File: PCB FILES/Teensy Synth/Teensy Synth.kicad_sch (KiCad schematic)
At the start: 102 parts, among them J1 Conn_01x05, SW1 SW_Push, SW10 SW_Push, SW11 SW_Push, SW12 SW_Push, SW13 SW_Push, SW14 SW_Push, SW15 SW_Push, SW16 SW_Push, SW17 SW_Push, SW18 SW_Push, SW19 SW_Push, SW2 SW_Push, SW20 SW_Push, SW21 SW_Push, SW22 SW_Push, SW23 SW_Push, SW24 SW_Push, SW25 SW_Push, SW26 SW_Push, SW27 SW_Push, SW28 SW_Push, SW29 SW_Push, SW3 SW_Push, SW30 SW_Push, SW31 SW_Push, SW32 SW_Push, SW33 SW_Push, SW34 SW_Push, SW35 SW_Push, SW36 SW_Push, SW37 SW_Push, SW38 SW_Push, SW39 SW_Push, SW4 SW_Push, SW40 SW_Push, SW41 SW_Push, SW42 SW_Push, SW43 SW_Push, SW44 SW_Push, SW45 SW_Push, SW46 SW_Push, SW47 SW_Push, SW48 RotaryEncoder, SW49 RotaryEncoder, SW5 SW_Push, SW50 RotaryEncoder, SW51 RotaryEncoder, SW52 RotaryEncoder, SW6 SW_Push, SW7 SW_Push, SW8 SW_Push, SW9 SW_Push, U1 Teensy4.1, U2 RP2040

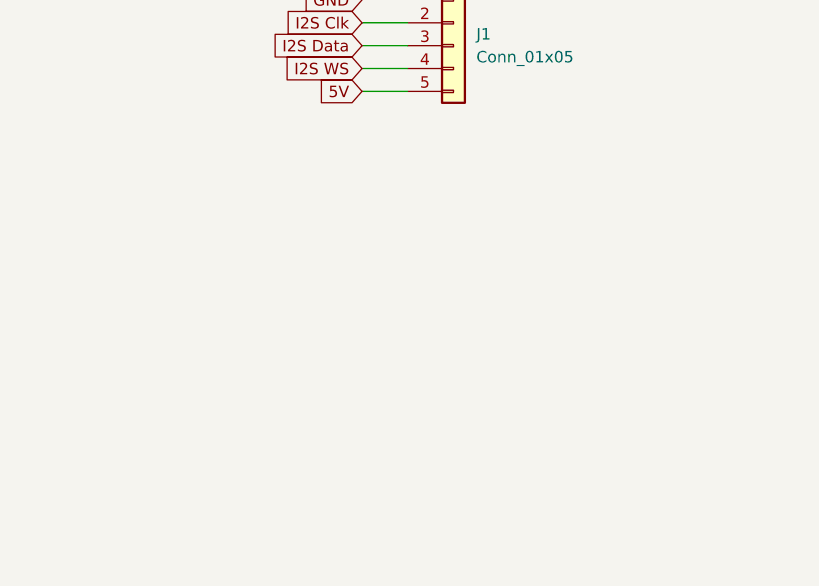
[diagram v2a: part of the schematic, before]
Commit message: Added Screen Pins
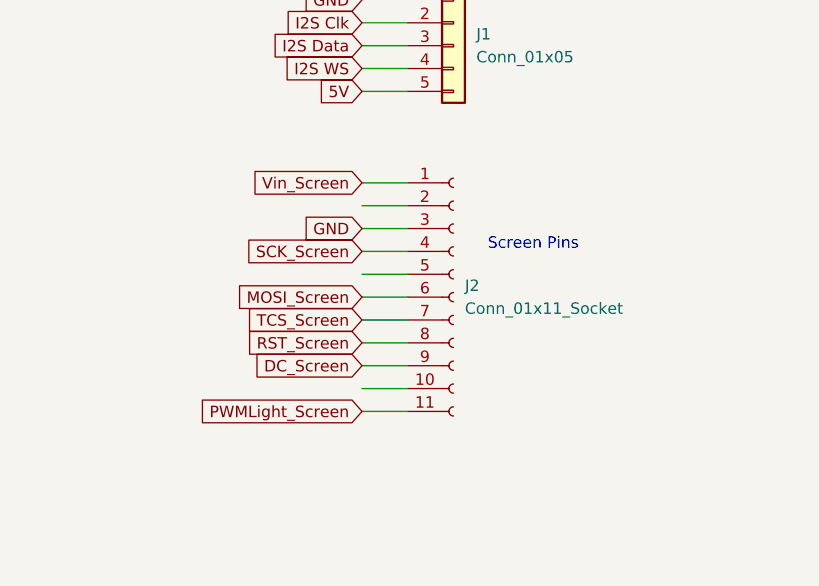
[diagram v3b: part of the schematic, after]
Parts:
- added J2: Conn_01x11_Socket, symbol Connector:Conn_01x11_Socket
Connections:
- net GND: now also J2.3 (Pin_3)
- new net DC_Screen: J2.9 (Pin_9)
- new net MOSI_Screen: J2.6 (Pin_6)
- new net PWMLight_Screen: J2.11 (Pin_11)
- new net RST_Screen: J2.8 (Pin_8)
- new net SCK_Screen: J2.4 (Pin_4)
- new net TCS_Screen: J2.7 (Pin_7)
- new net Vin_Screen: J2.1 (Pin_1)
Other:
- note added: "Screen Pins"
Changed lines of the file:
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@@
   (junction (at 254 330.2) (diameter 0) (color 0 0 0 0)
   )
+  (wire (pts (xy 312.42 63.5) (xy 317.5 63.5))
+    (stroke (width 0) (type default))
+  )
   (wire (pts (xy 86.36 322.58) (xy 86.36 342.9))
     (stroke (width 0) (type default))
@@
     (stroke (width 0) (type default))
   )
+  (wire (pts (xy 312.42 68.58) (xy 317.5 68.58))
+    (stroke (width 0) (type default))
+  )
   (wire (pts (xy 314.96 284.48) (xy 314.96 297.18))
     (stroke (width 0) (type default))
   )
+  (wire (pts (xy 312.42 73.66) (xy 317.5 73.66))
+    (stroke (width 0) (type default))
+  )
   (wire (pts (xy 152.4 304.8) (xy 177.8 304.8))
     (stroke (width 0) (type default))
@@
     (stroke (width 0) (type default))
   )
+  (wire (pts (xy 312.42 76.2) (xy 317.5 76.2))
+    (stroke (width 0) (type default))
+  )
   (wire (pts (xy 177.8 330.2) (xy 203.2 330.2))
     (stroke (width 0) (type default))
@@
     (stroke (width 0) (type default))
   )
+  (wire (pts (xy 312.42 66.04) (xy 317.5 66.04))
+    (stroke (width 0) (type default))
+  )
   (wire (pts (xy 416.56 284.48) (xy 416.56 297.18))
     (stroke (width 0) (type default))
@@
     (stroke (width 0) (type default))
   )
+  (wire (pts (xy 312.42 71.12) (xy 317.5 71.12))
+    (stroke (width 0) (type default))
+  )
   (wire (pts (xy 312.42 40.64) (xy 317.5 40.64))
     (stroke (width 0) (type default))
@@
     (stroke (width 0) (type default))
   )
+  (wire (pts (xy 312.42 78.74) (xy 317.5 78.74))
+    (stroke (width 0) (type default))
+  )
   (wire (pts (xy 365.76 297.18) (xy 365.76 322.58))
     (stroke (width 0) (type default))
@@
     (stroke (width 0) (type default))
   )
+  (wire (pts (xy 312.42 83.82) (xy 317.5 83.82))
+    (stroke (width 0) (type default))
+  )
   (wire (pts (xy 60.96 297.18) (xy 60.96 309.88))
     (stroke (width 0) (type default))
@@
     (stroke (width 0) (type default))
   )
+  (wire (pts (xy 312.42 81.28) (xy 317.5 81.28))
+    (stroke (width 0) (type default))
+  )
   (wire (pts (xy 304.8 330.2) (xy 330.2 330.2))
     (stroke (width 0) (type default))
@@
     (stroke (width 0) (type default))
   )
+  (wire (pts (xy 312.42 60.96) (xy 317.5 60.96))
+    (stroke (width 0) (type default))
+  )
   (wire (pts (xy 50.8 304.8) (xy 76.2 304.8))
     (stroke (width 0) (type default))
@@
     (stroke (width 0) (type default))
   )
+  (wire (pts (xy 312.42 58.42) (xy 317.5 58.42))
+    (stroke (width 0) (type default))
+  )
   (text "To Audio Board" (at 325.12 36.83 0)
     (effects (font (size 1.27 1.27)) (justify left bottom))
   )
+  (text "Screen Pins" (at 326.39 66.04 0)
+    (effects (font (size 1.27 1.27)) (justify left bottom))
+  )
   (global_label "Enc 2A" (shape input) (at 279.4 241.3 270) (fields_autoplaced)
     (effects (font (size 1.27 1.27)) (justify right))
@@
     )
   )
+  (global_label "SCK_Screen" (shape input) (at 312.42 66.04 180) (fields_autoplaced)
+    (effects (font (size 1.27 1.27)) (justify right))
+    (property "Intersheetrefs" "${INTERSHEET_REFS}" (at 298.3072 66.04 0)
+      (effects (font (size 1.27 1.27)) (justify right) hide)
+    )
+  )
   (global_label "Col 13" (shape input) (at 391.16 342.9 270) (fields_autoplaced)
     (effects (font (size 1.27 1.27)) (justify right))
@@
     )
   )
+  (global_label "PWMLight_Screen" (shape input) (at 312.42 83.82 180) (fields_autoplaced)
+    (effects (font (size 1.27 1.27)) (justify right))
+    (property "Intersheetrefs" "${INTERSHEET_REFS}" (at 293.2273 83.82 0)
+      (effects (font (size 1.27 1.27)) (justify right) hide)
+    )
+  )
   (global_label "Col 7" (shape input) (at 238.76 342.9 270) (fields_autoplaced)
     (effects (font (size 1.27 1.27)) (justify right))
@@
     )
   )
+  (global_label "MOSI_Screen" (shape input) (at 312.42 71.12 180) (fields_autoplaced)
+    (effects (font (size 1.27 1.27)) (justify right))
+    (property "Intersheetrefs" "${INTERSHEET_REFS}" (at 297.4605 71.12 0)
+      (effects (font (size 1.27 1.27)) (justify right) hide)
+    )
+  )
+  (global_label "TCS_Screen" (shape input) (at 312.42 73.66 180) (fields_autoplaced)
+    (effects (font (size 1.27 1.27)) (justify right))
+    (property "Intersheetrefs" "${INTERSHEET_REFS}" (at 298.6096 73.66 0)
+      (effects (font (size 1.27 1.27)) (justify right) hide)
+    )
+  )
   (global_label "Enc VA" (shape input) (at 152.4 241.3 270) (fields_autoplaced)
     (effects (font (size 1.27 1.27)) (justify right))
@@
     )
   )
+  (global_label "DC_Screen" (shape input) (at 312.42 78.74 180) (fields_autoplaced)
+    (effects (font (size 1.27 1.27)) (justify right))
+    (property "Intersheetrefs" "${INTERSHEET_REFS}" (at 299.5167 78.74 0)
+      (effects (font (size 1.27 1.27)) (justify right) hide)
+    )
+  )
   (global_label "Enc 3A" (shape input) (at 304.8 241.3 270) (fields_autoplaced)
     (effects (font (size 1.27 1.27)) (justify right))
@@
     )
   )
+  (global_label "Vin_Screen" (shape input) (at 312.42 58.42 180) (fields_autoplaced)
+    (effects (font (size 1.27 1.27)) (justify right))
+    (property "Intersheetrefs" "${INTERSHEET_REFS}" (at 299.2143 58.42 0)
+      (effects (font (size 1.27 1.27)) (justify right) hide)
+    )
+  )
   (global_label "Enc VB" (shape input) (at 157.48 241.3 270) (fields_autoplaced)
     (effects (font (size 1.27 1.27)) (justify right))
@@
     )
   )
+  (global_label "RST_Screen" (shape input) (at 312.42 76.2 180) (fields_autoplaced)
+    (effects (font (size 1.27 1.27)) (justify right))
+    (property "Intersheetrefs" "${INTERSHEET_REFS}" (at 298.6096 76.2 0)
+      (effects (font (size 1.27 1.27)) (justify right) hide)
+    )
+  )
+  (global_label "GND" (shape input) (at 312.42 63.5 180) (fields_autoplaced)
+    (effects (font (size 1.27 1.27)) (justify right))
+    (property "Intersheetrefs" "${INTERSHEET_REFS}" (at 305.5643 63.5 0)
+      (effects (font (size 1.27 1.27)) (justify right) hide)
+    )
+  )
   (global_label "5V" (shape input) (at 312.42 48.26 180) (fields_autoplaced)
     (effects (font (size 1.27 1.27)) (justify right))
@@
         )
       )
+    )
+  )
+  (symbol (lib_id "Connector:Conn_01x11_Socket") (at 322.58 71.12 0) (unit 1)
+    (in_bom yes) (on_board yes) (dnp no) (fields_autoplaced)
+    (property "Reference" "J2" (at 323.85 69.85 0)
+      (effects (font (size 1.27 1.27)) (justify left))
+    )
+    (property "Value" "Conn_01x11_Socket" (at 323.85 72.39 0)
+      (effects (font (size 1.27 1.27)) (justify left))
+    )
+    (property "Footprint" "" (at 322.58 71.12 0)
+      (effects (font (size 1.27 1.27)) hide)
+    )
+    (property "Datasheet" "~" (at 322.58 71.12 0)
+      (effects (font (size 1.27 1.27)) hide)
+    )
+    (pin "1")
+    (pin "10")
+    (pin "11")
+    (pin "2")
+    (pin "3")
+    (pin "4")
+    (pin "5")
+    (pin "6")
+    (pin "7")
+    (pin "8")
+    (pin "9")
+    (instances
+      (project "Teensy Synth"
+        (path "/c9e64777-b068-4bbd-bb2c-e1f5e825559e"
+          (reference "J2") (unit 1)
+        )
+      )

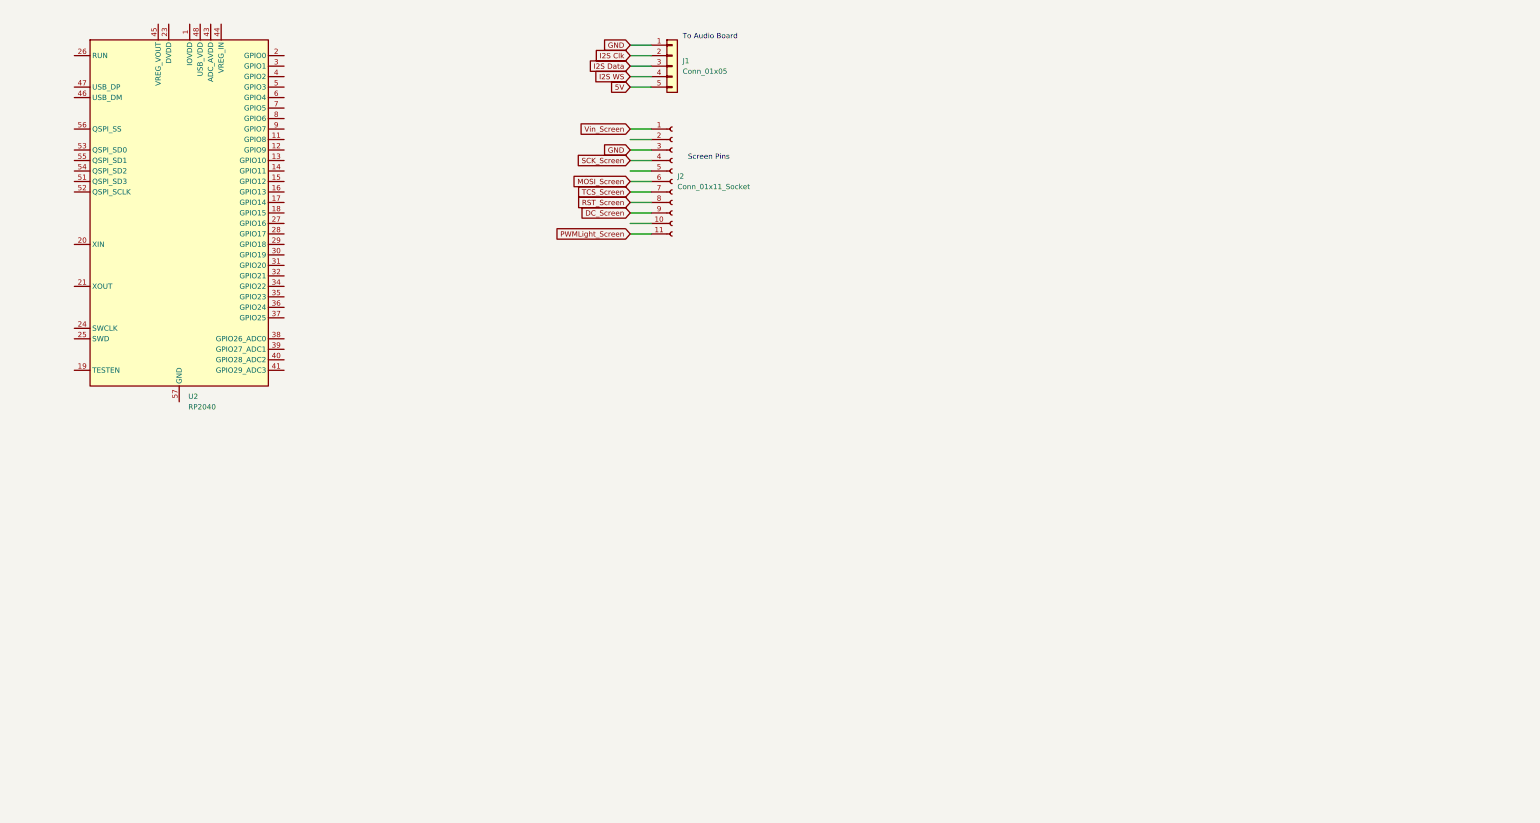
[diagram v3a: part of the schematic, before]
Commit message: Added EncoderDaughterboard and Firmware folders
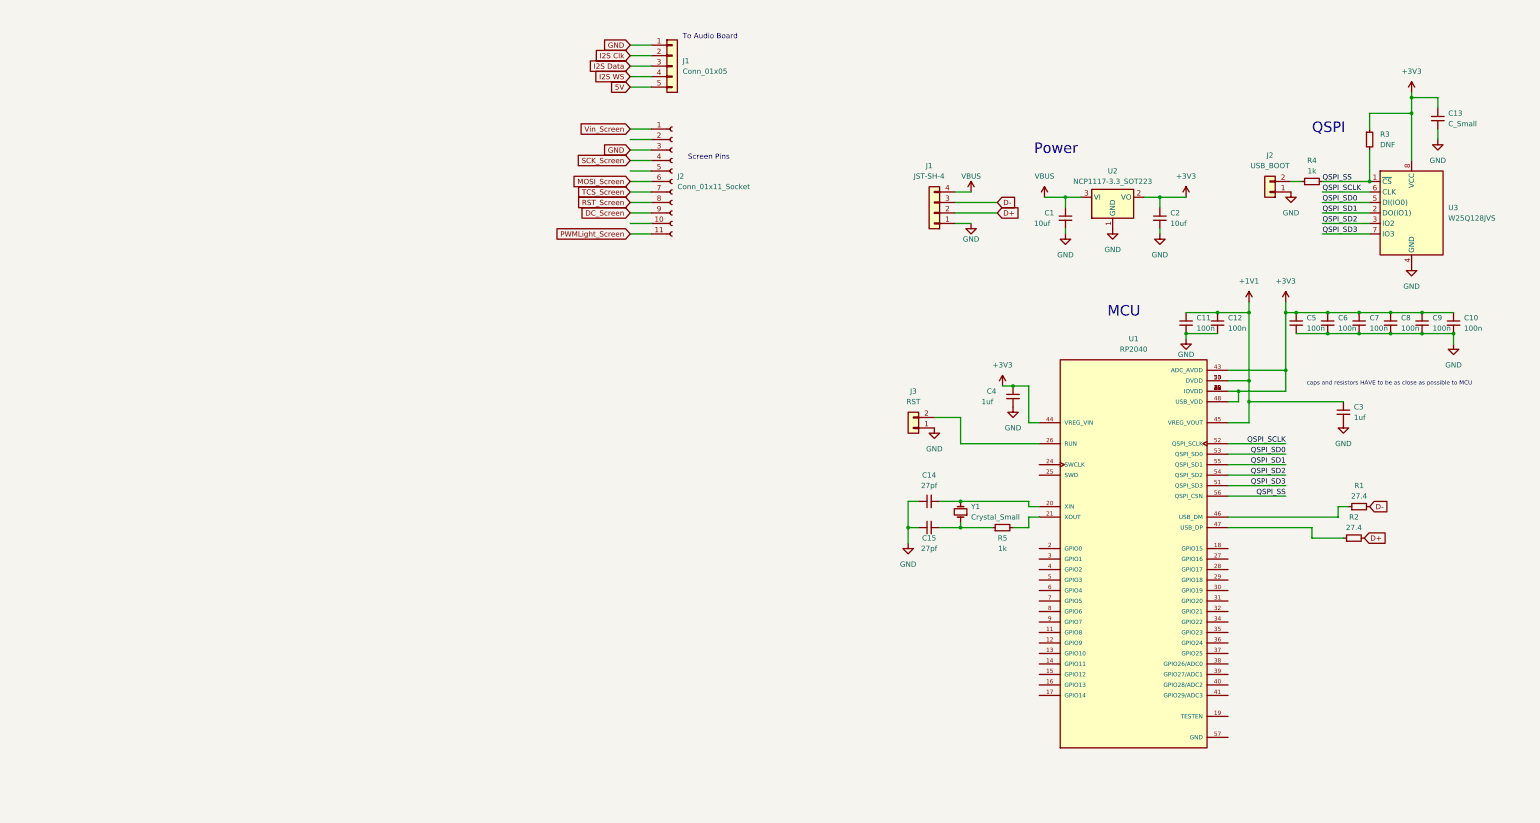
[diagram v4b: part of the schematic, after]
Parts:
- removed U2: RP2040, Package_DFN_QFN:QFN-56-1EP_7x7mm_P0.4mm_EP3.2x3.2mm, symbol MCU_RaspberryPi:RP2040
- added C1, C2: 10uf, symbol Device:C_Small
- added C10, C11, C12, C5, C6, C7, C8, C9: 100n, symbol Device:C_Small
- added C13: C_Small, symbol Device:C_Small
- added C14, C15: 27pf, symbol Device:C_Small
- added C3, C4: 1uf, symbol Device:C_Small
- added J1: JST-SH-4, symbol Connector_Generic:Conn_01x04
- added J2: USB_BOOT, symbol Connector_Generic:Conn_01x02
- added J3: RST, symbol Connector_Generic:Conn_01x02
- added R1, R2: 27.4, symbol Device:R_Small
- added R3: DNF, symbol Device:R_Small
- added R4, R5: 1k, symbol Device:R_Small
- added U1: RP2040, RP2040:QFN40P700X700X90-57N, symbol RP2040:RP2040
- added U2: NCP1117-3.3_SOT223, Package_TO_SOT_SMD:SOT-223-3_TabPin2, symbol Regulator_Linear:NCP1117-3.3_SOT223
- added U3: W25Q128JVS, Package_SO:SOIC-8_5.23x5.23mm_P1.27mm, symbol Memory_Flash:W25Q128JVS
- added Y1: Crystal_Small, symbol Device:Crystal_Small
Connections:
- net GND: now also C1.2, C10.2, C11.2, C12.2, C13.2, C14.1, C15.1, C2.2, C3.2, C4.2, C5.2, C6.2, C7.2, C8.2, C9.2, J1.1 (Pin_1), J2.1 (Pin_1), J3.1 (Pin_1), U2.1 (GND), U3.4 (GND)
- new net: C14.2, U1.20 (XIN), Y1.2
- new net: C15.2, R5.1, Y1.1
- new net: R2.1, U1.47 (USB_DP)
- new net: J3.2 (Pin_2), U1.26 (RUN)
- new net: J2.2 (Pin_2), R4.1
- new net: R5.2, U1.21 (XOUT)
- new net: R1.1, U1.46 (USB_DM)
- new net +1V1: C11.1, C12.1, C3.1, U1.23 (DVDD), U1.45 (VREG_VOUT), U1.50 (DVDD)
- new net +3V3: C10.1, C13.1, C2.1, C4.1, C5.1, C6.1, C7.1, C8.1, C9.1, R3.1, U1.1 (IOVDD), U1.10 (IOVDD), U1.22 (IOVDD), U1.33 (IOVDD), U1.42 (IOVDD), U1.43 (ADC_AVDD), U1.44 (VREG_VIN), U1.48 (USB_VDD), U1.49 (IOVDD), U2.2 (VO), U3.8 (VCC)
- new net D+: J1.2 (Pin_2), R2.2
- new net D-: J1.3 (Pin_3), R1.2
- new net QSPI_SCLK: U1.52 (QSPI_SCLK), U3.6 (CLK)
- new net QSPI_SD0: U1.53 (QSPI_SD0), U3.5 (DI(IO0))
- new net QSPI_SD1: U1.55 (QSPI_SD1), U3.2 (DO(IO1))
- new net QSPI_SD2: U1.54 (QSPI_SD2), U3.3 (IO2)
- new net QSPI_SD3: U1.51 (QSPI_SD3), U3.7 (IO3)
- new net QSPI_SS: R3.2, R4.2, U1.56 (QSPI_CSN), U3.1 (~{CS})
- new net VBUS: C1.1, J1.4 (Pin_4), U2.3 (VI)
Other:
- note added: "MCU"
- note added: "Power"
- note added: "QSPI"
- note added: "caps and resistors HAVE to be as close as possible to MCU"

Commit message: THE COMMIT TO END ALL COMMITS
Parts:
- removed J1: JST-SH-4, symbol Connector_Generic:Conn_01x04
- added J4: Conn_01x04, symbol Connector_Generic:Conn_01x04
- added R6: 16k, symbol Device:R_Small
- added U2: TPS61090, Package_DFN_QFN:Texas_S-PVQFN-N16_EP2.7x2.7mm_ThermalVias, symbol Regulator_Switching:TPS61090
- added U6: MCP73871, Package_DFN_QFN:QFN-20-1EP_4x4mm_P0.5mm_EP2.5x2.5mm, symbol Battery_Management:MCP73871
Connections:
- net GND: now also U1.47 (GND), J4.1 (Pin_1), R6.2, U6.10 (V_{SS}), U6.11 (V_{SS}), U6.21 (V_{SS})
- net +5V: now reaches U1.48 (VIN)
- new net: U6.1 (OUT), U6.20 (OUT)
- new net: R6.1, U6.5 (THERM)
- new net VBAT: U6.14 (V_{BAT}), U6.15 (V_{BAT}), U6.16 (V_{BAT_SENSE})
- new net VUSB: J4.4 (Pin_4), U6.18 (IN), U6.19 (IN), U6.4 (PROG2)
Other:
- note added: "Battery Circuitry"
- note added: "Switches + Encoders"
- note added: "To RP2040"
- moved on the sheet: C1, C10, C11, C12, C13, C14, C15, C2, C3, C4, C5, C6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
